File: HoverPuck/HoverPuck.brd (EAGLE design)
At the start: 50 x 20 mm, 14 parts, among them Q1 FDME, Q2 FDME, U1 EFM8BB1.QFN20, U2 TPS62177.DQC

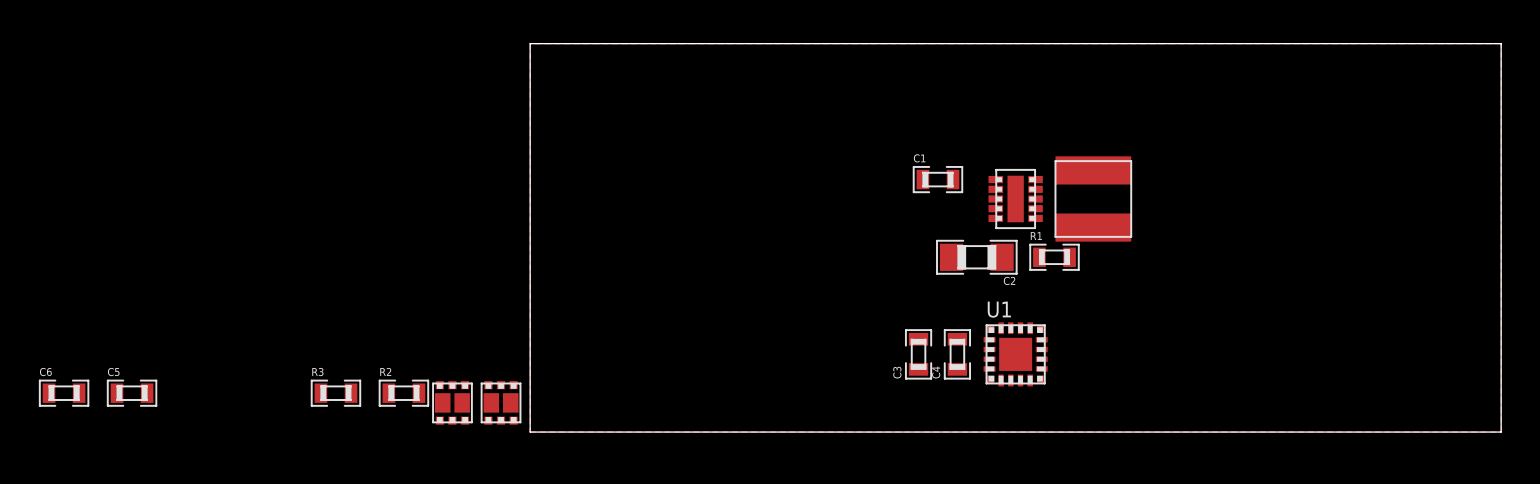
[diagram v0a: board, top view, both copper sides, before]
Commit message: Schematic seems about done and layout of components looks promising Next step will be the actual routing
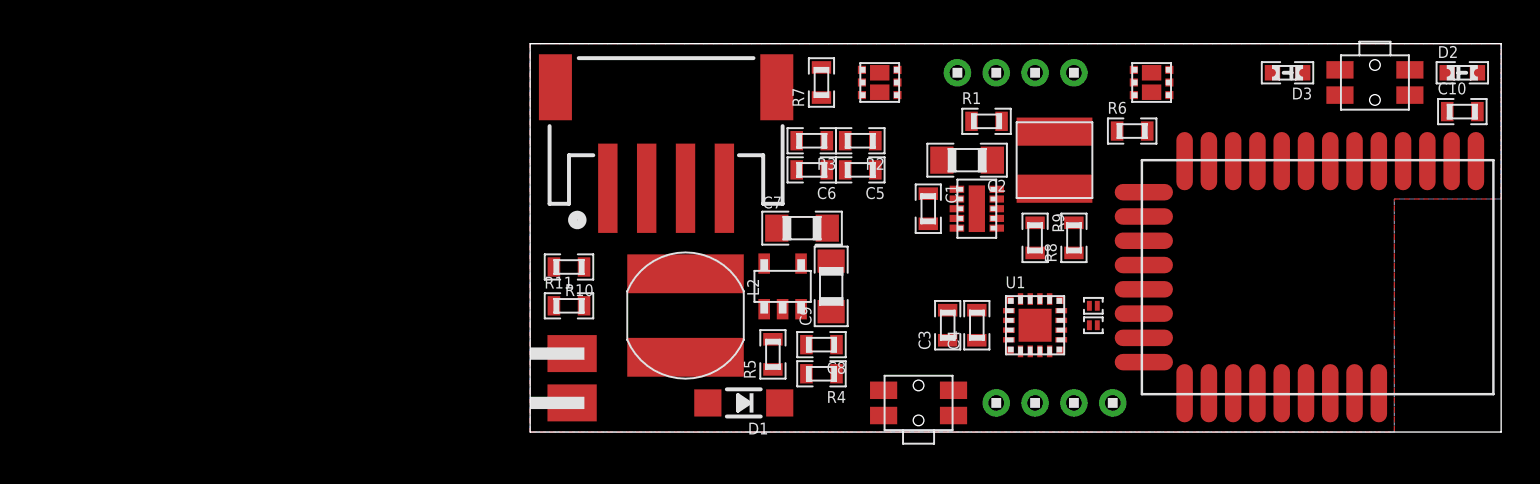
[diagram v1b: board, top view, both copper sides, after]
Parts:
- added B1, B2: (no value), alps:SKSCLDE010
- added C10: 1uF, standardparts:0603
- added C7, C9: 4.7uF, standardparts:0805
- added C8: 150pF, standardparts:0603
- added D1: MBR0530T1G, microbuilder:SOD-123
- added D2, D3: (no value), standardparts:0603.LED
- added J1, J4: 1X4, headers(2mm):1X4
- added J2: 1X2, headers.edge(.1in):1X2
- added J3: (no value), microbuilder:JSTPH4
- added J6, J7: (no value), solderjumper:2.SML.PASTE
- added L2: 10uH, bourns:SRN6045
- added R10, R11, R6, R7, R8, R9: 1k, standardparts:0603
- added R4: 205k, standardparts:0603
- added R5: 13.3k, standardparts:0603
- added U3: LM2731.DBV, packages(ti):DBV.5
- added U4: BLE112-A, SparkFun-RF:BLE112-A
- moved C6 40.2 mm to (14.5, 13.5), turned to 180 degrees
- moved C5 39.2 mm to (17.0, 13.5), turned to 180 degrees
- moved Q1 37.3 mm to (32.0, 18.0), turned to 270 degrees
- moved R3 27.7 mm to (14.5, 15.0), turned to 180 degrees
- moved Q2 27.5 mm to (18.0, 18.0), turned to 90 degrees
- moved R2 26.9 mm to (17.0, 15.0), turned to 180 degrees
- moved R1 7.83 mm to (23.5, 16.0)
- moved C2 5.02 mm to (22.5, 14.0)
- moved L1 2.83 mm to (27.0, 14.0)
- moved C3 2.12 mm to (21.5, 5.50)
- moved U2 2.06 mm to (23.0, 11.5)
- moved C4 1.80 mm to (23.0, 5.50)
- moved U1 1.80 mm to (26.0, 5.50)
- moved C1 1.58 mm to (20.5, 11.5), turned to 270 degrees
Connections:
- removed net LED: U1.1
- new net 10V: C5.2, C6.1, J4.2, J4.3, R2.2, R3.1
- new net 1S_DBG: J3.2, R10.1
- new net 20V: C5.1, C8.1, C9.1, D1.C, Q1.6, Q1.PAD@1, Q2.6, Q2.PAD@1, R2.1, R4.1
- new net EN: D2.P$1, D3.P$1, U1.1, U3.4
- new net N$10: J6.1, U4.24
- new net N$11: J7.1, U4.23
- new net N$12: B2.1, B2.2, U4.29
- new net N$5: D1.A, L2.2, U3.1
- new net N$7: C8.2, R4.2, R5.1, U3.3
- new net N$8: D3.P$2, R9.1
- new net N$9: R10.2, R11.1
- net !RST: now also B1.3, B1.4, J1.2
- net 3.3V: now also C10.1, J1.1, U4.2, U4.20, U4.3
- net ADC0: now also R11.2
- net C2D: now also J1.3
- net GND: now also B1.1, B1.2, B2.3, B2.4, C10.2, C7.2, C9.2, J1.4, J2.1, J3.1, R5.2, R6.2, R7.2, R8.2, R9.2, U3.2, U4.1, U4.10, U4.21, U4.30
- net N$1: now also J4.1
- net N$2: now also J4.4
- net N$4: now also D2.P$2, R8.1; no longer C5.2, C6.1, R2.2, R3.1
- net PWM0: now also Q1.2, Q1.5, R6.1
- net PWM1: now also Q2.2, Q2.5, R7.1
- net RXI: now also J6.2
- net TXO: now also J7.2
- net VBAT: now also C7.1, J2.2, L2.1, U3.5
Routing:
- added copper zone on layer 16, net GND

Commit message: A majority of routing completed. Switching regulators now completed. Minor MCU signals still needed, as well as labeling.
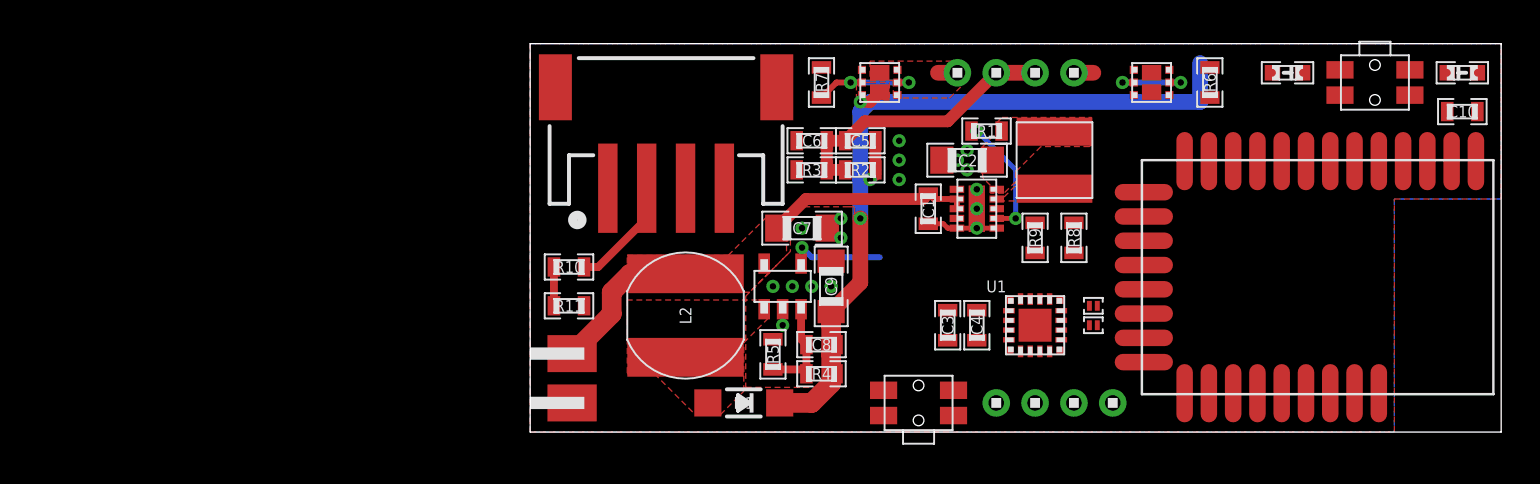
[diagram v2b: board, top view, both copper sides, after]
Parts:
- moved R6 4.72 mm to (35.0, 18.0), turned to 90 degrees
- moved C5 1.50 mm to (17.0, 15.0)
- moved C6 1.50 mm to (14.5, 15.0)
- moved R2 1.50 mm to (17.0, 13.5)
- moved R3 1.50 mm to (14.5, 13.5)
- moved R1 0.50 mm to (23.5, 15.5)
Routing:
- net 20V: track 0.00 -> 43.9 mm, vias 0 -> 3
- net VBAT: track 0.00 -> 18.8 mm
- net 10V: track 0.00 -> 14.6 mm
- net N$6: track 0.00 -> 6.58 mm, vias 0 -> 2
- net PWM1: track 0.00 -> 5.99 mm, vias 0 -> 2
- net 1S_DBG: track 0.00 -> 5.81 mm
- net N$7: track 0.00 -> 5.26 mm
- net EN: track 0.00 -> 5.05 mm, vias 0 -> 1
- net PWM0: track 0.00 -> 4.17 mm, vias 0 -> 2
- net GND: track 0.00 -> 3.59 mm, vias 0 -> 17
- net N$9: track 0.00 -> 2.00 mm
- net N$2: track 0.00 -> 1.00 mm
- net N$1: track 0.00 -> 1.00 mm
- added copper zone on layer 1, net 20V
- added copper zone on layer 1, net 3.3V
- added copper zone on layer 1, net N$2
- added copper zone on layer 1, net N$3
- added copper zone on layer 1, net N$5
- added copper zone on layer 1, net VBAT

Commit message: Updated board file with more routing and placement
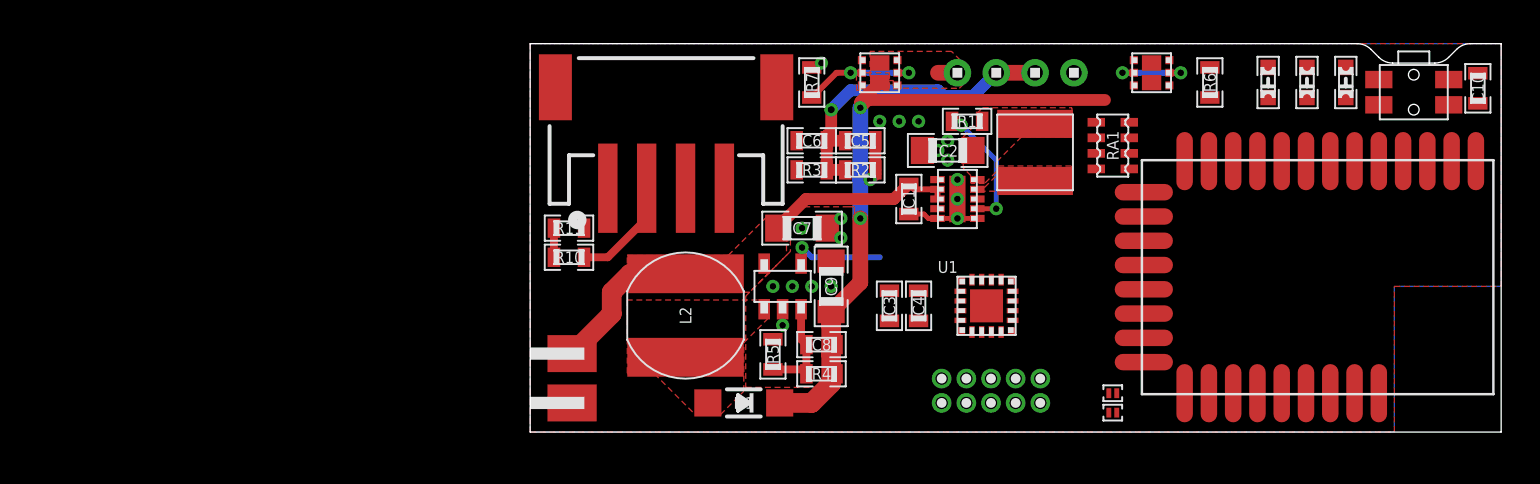
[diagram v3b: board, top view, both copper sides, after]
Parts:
- removed B2: (no value), alps:SKSCLDE010
- removed J1: 1X4, headers(2mm):1X4
- removed R8, R9: 1k, standardparts:0603
- added D4: (no value), standardparts:0603.LED
- added RA1: (no value), resistorarray:0603.4.C
- added U$38, U$39: 1X5, headers(.05in):1X5
- R10, R11, R6, R7: value 1k -> 10k
- moved B1 30.1 mm to (45.5, 17.5), turned to 180 degrees
- moved D2 6.02 mm to (42.0, 18.0), turned to 90 degrees
- moved J6 4.61 mm to (30.0, 2.00)
- moved J7 4.61 mm to (30.0, 1.00)
- moved R11 4.00 mm to (2.00, 10.5)
- moved C3 3.16 mm to (18.5, 6.50)
- moved C4 3.16 mm to (20.0, 6.50)
- moved U1 2.69 mm to (23.5, 6.50)
- moved C10 1.44 mm to (48.8, 17.7), turned to 270 degrees
- moved C1 1.12 mm to (19.5, 12.0)
- moved C2 1.12 mm to (21.5, 14.5)
- moved D3 1.12 mm to (40.0, 18.0), turned to 90 degrees
- moved R1 1.12 mm to (22.5, 16.0)
- moved U2 1.12 mm to (22.0, 12.0)
- moved L1 1.08 mm to (26.0, 14.4)
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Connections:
- removed net !RST: B1.3, B1.4, J1.2, U1.5
- removed net C2D: J1.3, U1.6
- removed net EN: D2.P$1, D3.P$1, U1.1, U3.4
- removed net N$12: B2.1, B2.2, U4.29
- new net 20V_EN: RA1.4, U1.1, U3.4
- new net BLE_!RST: RA1.7, U$38.4, U1.15, U4.29
- new net BLE_DC: U$38.2, U4.4
- new net BLE_DD: U$39.2, U4.5
- new net EFM8_C2CK: B1.3, B1.4, U$39.3, U1.5
- new net EFM8_C2D: U$38.3, U1.6
- new net STATUS: RA1.6, U1.16
- net 3.3V: now also RA1.2, RA1.8, U$38.5, U$39.1; no longer J1.1
- net ADC0: now also R10.2, R11.1; no longer R11.2
- net GND: now also D2.P$2, D3.P$2, D4.P$2, R11.2, U$38.1, U$39.5; no longer B2.3, B2.4, J1.4, R8.2, R9.2
- net N$4: now also D2.P$1, RA1.1; no longer D2.P$2, R8.1
- net N$8: now also D3.P$1, RA1.3; no longer D3.P$2, R9.1
- net N$9: now also D4.P$1, RA1.5; no longer R10.2, R11.1
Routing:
- net 20V: track 43.9 -> 37.2 mm
- net EN: track 5.05 -> 0.00 mm, vias 1 -> 0
- net 20V_EN: track 0.00 -> 5.05 mm, vias 0 -> 1
- net 10V: track 14.6 -> 16.6 mm, vias 0 -> 1
- net N$9: track 2.00 -> 0.00 mm
- net ADC0: track 0.00 -> 1.50 mm
- net N$1: track 1.00 -> 0.00 mm
- net VBAT: track 18.8 -> 18.0 mm
- net PWM1: track 5.99 -> 6.70 mm
- net GND: vias 17 -> 18
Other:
- outline, holes or cut-outs redrawn

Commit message: Completed v1 of HoverPuck PCB
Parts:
- added J1: (no value), solderjumper:2.SML.PASTE
- added TP1, TP2, TP3, TP4: TPTP06R, testpad:TP06R
- moved J7 8.73 mm to (26.5, 9.00)
- moved J6 6.95 mm to (26.5, 8.00)
- moved D2 4.45 mm to (37.6, 18.0)
- moved D4 3.17 mm to (41.2, 18.0)
- moved C3 0.64 mm to (19.1, 6.50)
- moved C4 0.64 mm to (20.6, 6.50)
- moved D3 0.63 mm to (39.4, 18.0)
- moved R6 0.50 mm to (35.5, 18.0)
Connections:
- removed net N$9 (its old number): D4.P$1, RA1.5
- new net N$12: J1.1, U1.1
- new net N$8: D4.P$1, RA1.1
- net 20V: now also TP2.TP
- net 20V_EN: now also U1.2; no longer U1.1
- net 3.3V: now also RA1.6, TP1.TP; no longer RA1.2
- net ADC0: now also J1.2; no longer U1.2
- net BLE_!RST: now also RA1.5, U1.14; no longer RA1.7, U1.15
- net N$4: now also RA1.7; no longer RA1.1
- net PWM0: now also Q2.2, Q2.5, R7.1, TP4.TP, U1.19; no longer Q1.2, Q1.5, R6.1, U1.20
- net PWM1: now also Q1.2, Q1.5, R6.1, TP3.TP, U1.16; no longer Q2.2, Q2.5, R7.1, U1.19
- net STATUS: now also RA1.2, U1.15; no longer RA1.6, U1.16
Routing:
- net 3.3V: track 0.00 -> 73.2 mm, vias 0 -> 8
- net EFM8_C2CK: track 0.00 -> 46.1 mm, vias 0 -> 3
- net BLE_!RST: track 0.00 -> 40.0 mm, vias 0 -> 2
- net BLE_DC: track 0.00 -> 28.2 mm, vias 0 -> 1
- net BLE_DD: track 0.00 -> 27.9 mm, vias 0 -> 1
- net N$12: track 0.00 -> 23.5 mm, vias 0 -> 2
- net PWM0: track 4.17 -> 24.4 mm, vias 2 -> 3
- net PWM1: track 6.70 -> 24.5 mm, vias 2 -> 4
- net 20V_EN: track 5.05 -> 22.0 mm, vias 1 -> 2
- net N$10: track 0.00 -> 15.1 mm, vias 0 -> 2
- net N$11: track 0.00 -> 15.0 mm, vias 0 -> 2
- net N$8: track 0.00 -> 11.8 mm
- net STATUS: track 0.00 -> 10.6 mm
- net N$9: track 0.00 -> 9.71 mm
- net N$4: track 0.00 -> 7.23 mm, vias 0 -> 2
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- added copper zone on layer 1, net N$1
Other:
- board text added: "20v"
- board text added: "3.3v"
- board text added: "Cruz Monrreal II AnomalousMaker.com"
- board text added: "HoverPuck"
- board text added: "PWM0"
- board text added: "PWM1"

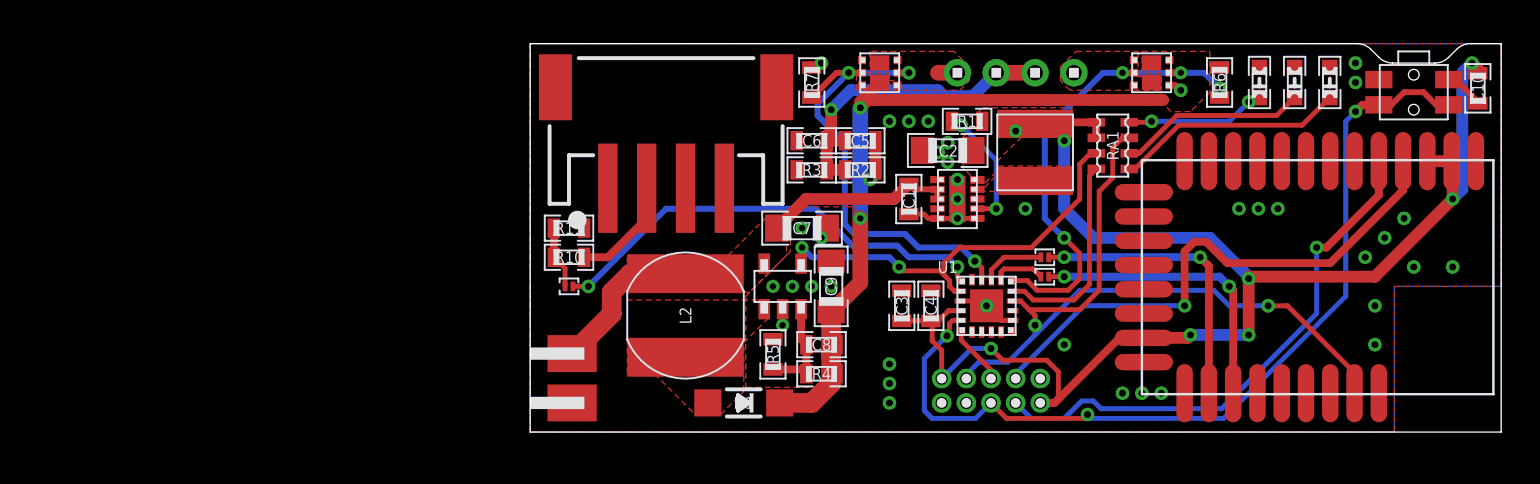
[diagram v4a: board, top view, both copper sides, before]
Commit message: Started v2 of the HoverPuck. Changed driver circuit, and moving things around. New driver circuit still needs to be confirmed functional.
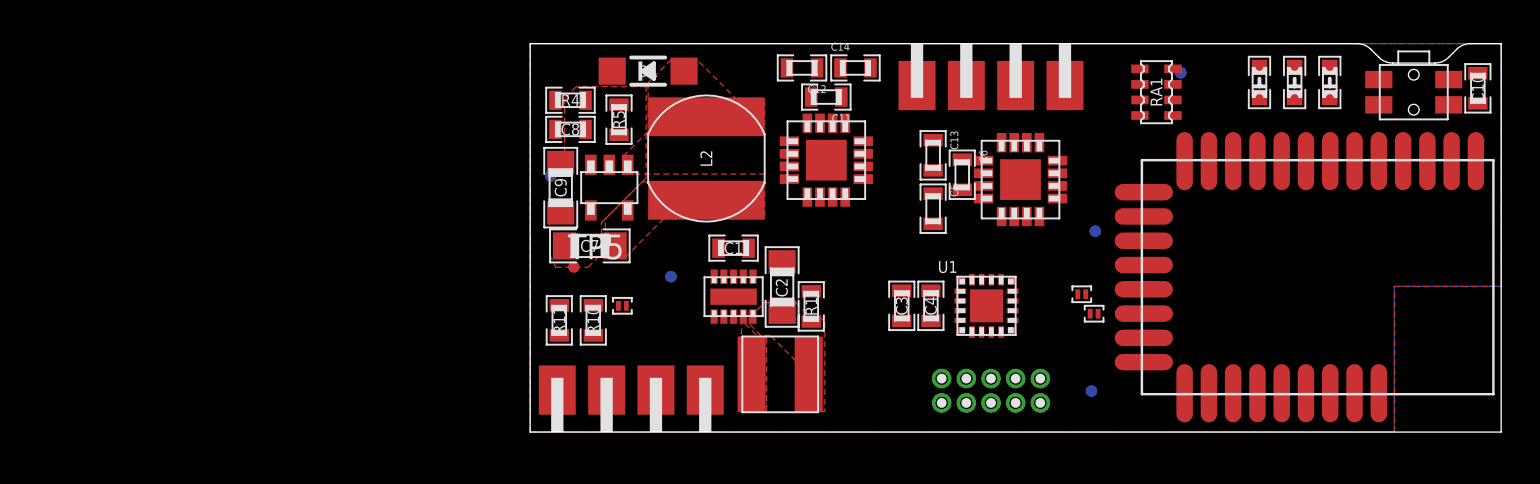
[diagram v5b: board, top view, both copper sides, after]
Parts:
- removed J3: (no value), microbuilder:JSTPH4
- removed J4: 1X4, headers(2mm):1X4
- removed Q1, Q2: FDME, fairchild:MICROFET.2X2
- removed R2, R3: 100k, standardparts:0603
- removed R6, R7: 10k, standardparts:0603
- added C11, C12, C13, C14: 0.1uF, standardparts:0603
- added MB0, MB1: 1X2, headers.edge(.1in):1X2
- added TP5, TP6: TPTP06R, testpad:TP06R
- added U5, U6: (no value), packages(ti):RTY.16
- C5, C6: value 1uF -> 0.1uF
- J2: value 1X2 -> 1X4; device headers.edge(.1in):1X2 -> headers.edge(.1in):1X4
- moved R4 19.1 mm to (2.08, 17.1), turned to 0 degrees
- moved D1 17.8 mm to (6.08, 18.6), turned to 0 degrees
- moved L1 17.4 mm to (12.9, 2.97), turned to 0 degrees
- moved C8 17.0 mm to (2.08, 15.6), turned to 0 degrees
- moved TP2 16.1 mm to (1.06, 13.2), turned to 270 degrees
- moved TP4 15.1 mm to (29.1, 10.3)
- moved C9 14.8 mm to (1.57, 12.6), turned to 270 degrees
- moved R5 14.5 mm to (4.58, 16.1), turned to 270 degrees
- moved TP1 13.9 mm to (28.9, 2.11)
- moved U2 12.6 mm to (10.5, 6.97), turned to 270 degrees
- moved R1 12.5 mm to (14.5, 6.47), turned to 270 degrees
- moved C2 11.0 mm to (13.0, 7.47), turned to 90 degrees
- moved C7 11.0 mm to (3.08, 9.59), turned to 180 degrees
- moved U3 10.3 mm to (4.08, 12.6), turned to 270 degrees
- moved C1 9.37 mm to (10.5, 9.47), turned to 180 degrees
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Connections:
- removed net 10V: C5.2, C6.1, J4.2, J4.3, R2.2, R3.1
- new net 12V: C12.1, C13.1, C14.1, C5.1, U5.8, U6.8
- new net EN_20V: U5.3, U6.3
- new net N$13: MB0.1, U5.6
- new net N$14: MB0.2, U5.9
- new net N$15: MB1.1, U6.6
- new net N$16: MB1.2, U6.9
- new net N$17: C6.1, U5.10
- new net N$18: C6.2, U5.11
- new net N$19: C11.2, U6.11
- new net N$20: C11.1, U6.10
- net 1S_DBG: now also J2.3; no longer J3.2
- net 20V: no longer C5.1, Q1.6, Q1.PAD@1, Q2.6, Q2.PAD@1, R2.1
- net 20V_EN: now also TP5.TP
- net 3.3V: now also U5.16, U5.4, U6.16, U6.4
- net GND: now also C13.2, C14.2, J2.4, TP6.TP, U5.12, U5.2, U5.7, U5.PAD, U6.12, U6.2, U6.7, U6.PAD; no longer C6.2, J2.1, J3.1, Q1.4, Q2.4, R3.2, R6.2, R7.2
- net N$1: now also C12.2, U6.13; no longer J4.1, Q1.1, Q1.3, Q1.PAD@2
- net N$2: now also C5.2, U5.13; no longer J4.4, Q2.1, Q2.3, Q2.PAD@2
- net PWM0: now also TP3.TP, U5.1; no longer Q2.2, Q2.5, R7.1, TP4.TP
- net PWM1: now also TP4.TP, U6.1; no longer Q1.2, Q1.5, R6.1, TP3.TP
- net VBAT: now also J2.1; no longer J2.2
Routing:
- net 3.3V: track 73.2 -> 0.00 mm, vias 8 -> 0
- net EFM8_C2CK: track 46.1 -> 0.00 mm, vias 3 -> 0
- net 20V: track 40.2 -> 0.00 mm, vias 3 -> 0
- net BLE_!RST: track 40.0 -> 0.00 mm, vias 2 -> 0
- net BLE_DC: track 28.2 -> 0.00 mm, vias 1 -> 0
- net BLE_DD: track 27.9 -> 0.00 mm, vias 1 -> 0
- net PWM1: track 24.5 -> 0.00 mm, vias 4 -> 0
- net PWM0: track 24.4 -> 0.00 mm, vias 3 -> 0
- net N$12: track 23.5 -> 0.00 mm, vias 2 -> 0
- net 20V_EN: track 22.0 -> 0.00 mm, vias 2 -> 0
- net VBAT: track 18.0 -> 0.00 mm
- net 10V: track 16.6 -> 0.00 mm, vias 1 -> 0
- net N$10: track 15.1 -> 0.00 mm, vias 2 -> 0
- net N$11: track 15.0 -> 0.00 mm, vias 2 -> 0
- net N$8: track 11.8 -> 0.00 mm
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- removed copper zone on layer 1, net 20V
- removed copper zone on layer 1, net N$1
- removed copper zone on layer 1, net N$2
